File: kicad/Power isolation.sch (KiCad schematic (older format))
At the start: 0 parts

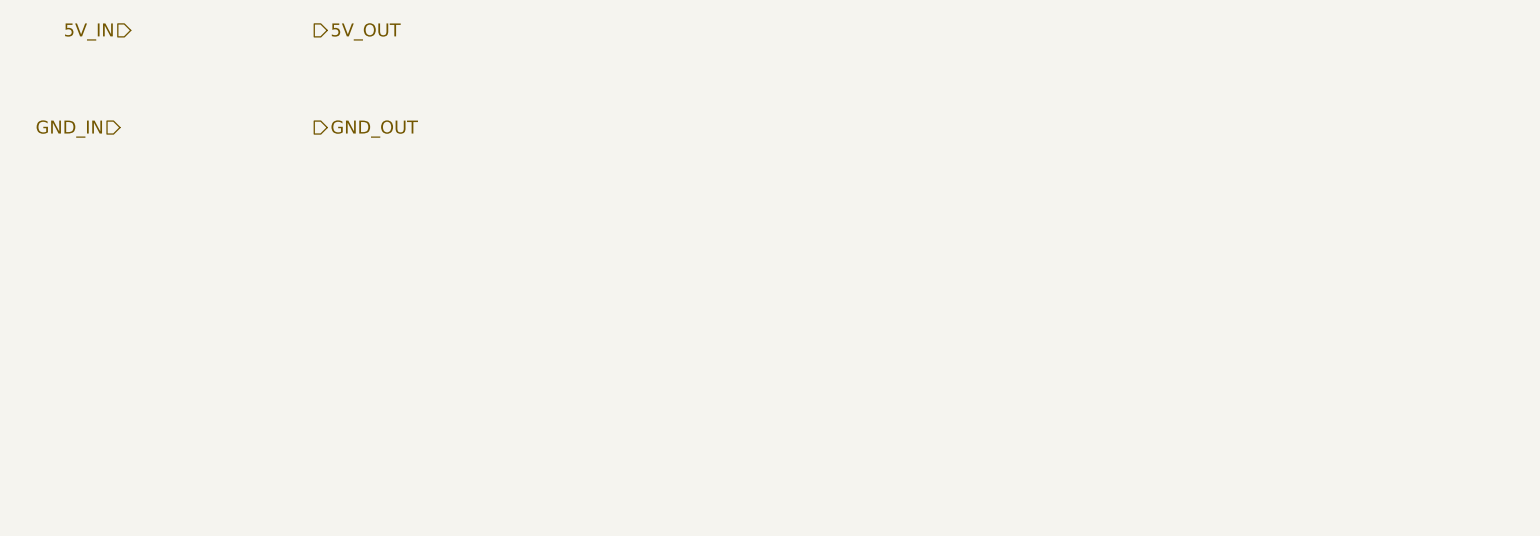
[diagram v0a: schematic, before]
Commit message: Completed data and power isolation sheets
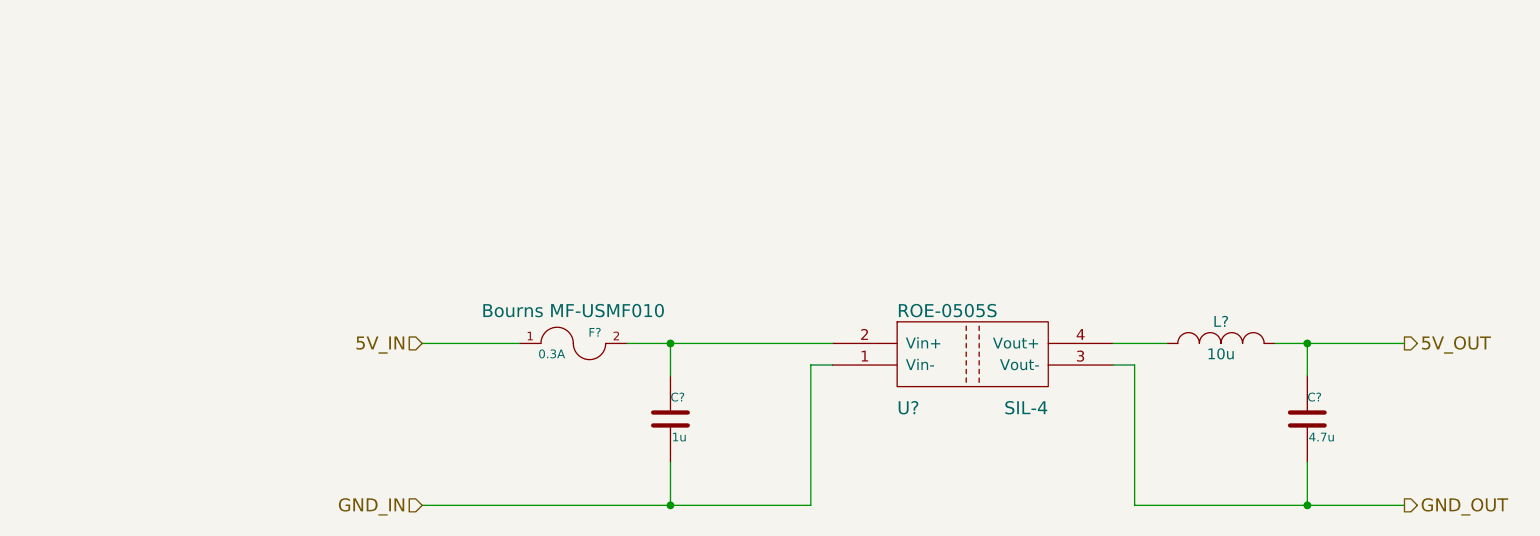
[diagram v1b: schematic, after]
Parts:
- added C?: 4.7u, ~, symbol C
- added C?: 1u, ~, symbol C
- added F?: 0.3A, ~, symbol FUSE
- added L?: 10u, ~, symbol INDUCTOR_SMALL
- added U?: ROE-0505S, SIL-4, symbol ROE-0505S
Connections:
- net 5V_IN: now also F?.1
- net 5V_OUT: now also C?.1, L?.2
- net GND_IN: now also C?.2, U?.1 (Vin-)
- net GND_OUT: now also C?.2, U?.3 (Vout-)
- new net: C?.1, F?.2, U?.2 (Vin+)
- new net: L?.1, U?.4 (Vout+)
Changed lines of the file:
@@
 LIBS:+5v_iso
 LIBS:gnd_iso
+LIBS:roe-0505s
+LIBS:si8660
 LIBS:Main-cache
 EELAYER 27 0
@@
 $Descr A4 11693 8268
 encoding utf-8
-Sheet 6 8
+Sheet 5 8
 Title ""
 Date "22 jun 2014"
@@
 Comment4 ""
 $EndDescr
-Text HLabel 2000 2150 0    60   Input ~ 0
+Text HLabel 3350 3600 0    60   Input ~ 0
 5V_IN
-Text HLabel 1950 2600 0    60   Input ~ 0
+Text HLabel 3350 4350 0    60   Input ~ 0
 GND_IN
-Text HLabel 2850 2150 2    60   Output ~ 0
+Text HLabel 7900 3600 2    60   Output ~ 0
 5V_OUT
-Text HLabel 2850 2600 2    60   Output ~ 0
+Text HLabel 7900 4350 2    60   Output ~ 0
 GND_OUT
+$Comp
+L ROE-0505S U?
+U 1 1 53AD64E4
+P 5900 3650
+F 0 "U?" H 5550 3400 60  0000 L CNN
+F 1 "ROE-0505S" H 5550 3850 60  0000 L CNN
+F 2 "SIL-4" H 6250 3400 60  0000 R CNN
+F 3 "" H 5900 3550 60  0000 C CNN
+	1    5900 3650
+	1    0    0    -1
+$EndComp
+$Comp
+L INDUCTOR_SMALL L?
+U 1 1 53AD651D
+P 7050 3600
+F 0 "L?" H 7050 3700 50  0000 C CNN
+F 1 "10u" H 7050 3550 50  0000 C CNN
+F 2 "~" H 7050 3600 60  0000 C CNN
+F 3 "~" H 7050 3600 60  0000 C CNN
+	1    7050 3600
+	1    0    0    -1
+$EndComp
+$Comp
+L C C?
+U 1 1 53AD6542
+P 7450 3950
+F 0 "C?" H 7450 4050 40  0000 L CNN
+F 1 "4.7u" H 7456 3865 40  0000 L CNN
+F 2 "~" H 7488 3800 30  0000 C CNN
+F 3 "~" H 7450 3950 60  0000 C CNN
+	1    7450 3950
+	1    0    0    -1
+$EndComp
+$Comp
+L C C?
+U 1 1 53AD6597
+P 4500 3950
+F 0 "C?" H 4500 4050 40  0000 L CNN
+F 1 "1u" H 4506 3865 40  0000 L CNN
+F 2 "~" H 4538 3800 30  0000 C CNN
+F 3 "~" H 4500 3950 60  0000 C CNN
+	1    4500 3950
+	1    0    0    -1
+$EndComp
+Wire Wire Line
+	4300 3600 4500 3600
+Wire Wire Line
+	4500 3600 5250 3600
+Wire Wire Line
+	5250 3700 5150 3700
+Wire Wire Line
+	7300 3600 7450 3600
+Wire Wire Line
+	7450 3600 7900 3600
+Wire Wire Line
+	6650 4350 7450 4350
+Wire Wire Line
+	7450 4350 7900 4350
+Wire Wire Line
+	7450 3750 7450 3600
+Connection ~ 7450 3600
+Wire Wire Line
+	6550 3600 6800 3600
+Wire Wire Line
+	6550 3700 6650 3700
+Wire Wire Line
+	6650 3700 6650 4350
+Wire Wire Line
+	7450 4150 7450 4350
+Connection ~ 7450 4350
+Wire Wire Line
+	5150 3700 5150 4350
+Wire Wire Line
+	5150 4350 4500 4350
+Wire Wire Line
+	4500 3600 4500 3750
+Wire Wire Line
+	4500 4150 4500 4350
+Connection ~ 4500 4350
+Connection ~ 4500 3600
+Wire Wire Line
+	3350 3600 3800 3600
+Wire Wire Line
+	4500 4350 3350 4350
+$Comp
+L FUSE F?
+U 1 1 53AD9F1B
+P 4050 3600
+F 0 "F?" H 4150 3650 40  0000 C CNN
+F 1 "0.3A" H 3950 3550 40  0000 C CNN
+F 2 "~" H 4050 3600 60  0000 C CNN
+F 3 "Bourns MF-USMF010" H 4050 3750 60  0000 C CNN
+	1    4050 3600
+	1    0    0    -1
+$EndComp
 $EndSCHEMATC

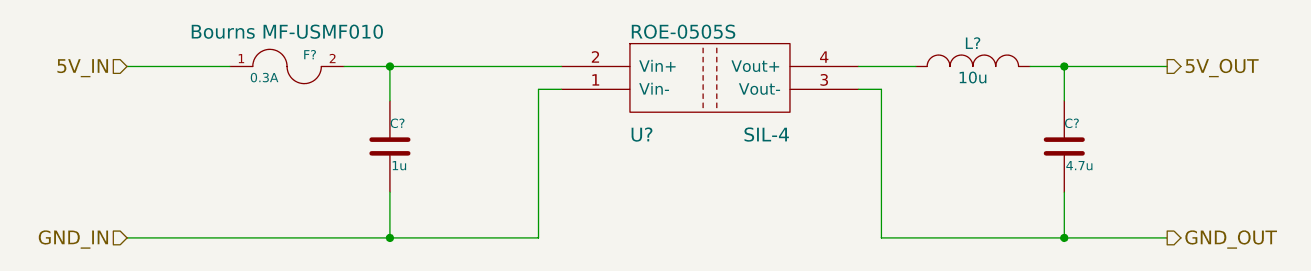
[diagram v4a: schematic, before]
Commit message: Netlist DRC pass - fixed pins types, incorrect connections, added PWRFLAGS
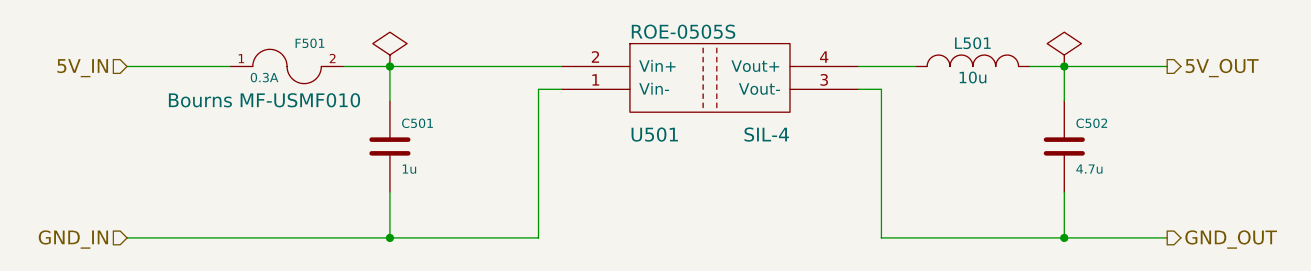
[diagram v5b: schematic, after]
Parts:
- gave numbers to parts that had none: 5
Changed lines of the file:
@@
 GND_OUT
 $Comp
-L ROE-0505S U?
+L ROE-0505S U501
 U 1 1 53AD64E4
 P 5900 3650
-F 0 "U?" H 5550 3400 60  0000 L CNN
+F 0 "U501" H 5550 3400 60  0000 L CNN
 F 1 "ROE-0505S" H 5550 3850 60  0000 L CNN
 F 2 "SIL-4" H 6250 3400 60  0000 R CNN
@@
 $EndComp
 $Comp
-L INDUCTOR_SMALL L?
+L INDUCTOR_SMALL L501
 U 1 1 53AD651D
 P 7050 3600
-F 0 "L?" H 7050 3700 50  0000 C CNN
+F 0 "L501" H 7050 3700 50  0000 C CNN
 F 1 "10u" H 7050 3550 50  0000 C CNN
 F 2 "~" H 7050 3600 60  0000 C CNN
@@
 $EndComp
 $Comp
-L C C?
+L C C502
 U 1 1 53AD6542
 P 7450 3950
-F 0 "C?" H 7450 4050 40  0000 L CNN
-F 1 "4.7u" H 7456 3865 40  0000 L CNN
+F 0 "C502" H 7500 4050 40  0000 L CNN
+F 1 "4.7u" H 7500 3850 40  0000 L CNN
 F 2 "~" H 7488 3800 30  0000 C CNN
 F 3 "~" H 7450 3950 60  0000 C CNN
@@
 $EndComp
 $Comp
-L C C?
+L C C501
 U 1 1 53AD6597
 P 4500 3950
-F 0 "C?" H 4500 4050 40  0000 L CNN
-F 1 "1u" H 4506 3865 40  0000 L CNN
+F 0 "C501" H 4550 4050 40  0000 L CNN
+F 1 "1u" H 4550 3850 40  0000 L CNN
 F 2 "~" H 4538 3800 30  0000 C CNN
 F 3 "~" H 4500 3950 60  0000 C CNN
@@
 $EndComp
 Wire Wire Line
-	4300 3600 4500 3600
-Wire Wire Line
-	4500 3600 5250 3600
+	4300 3600 5250 3600
 Wire Wire Line
 	5250 3700 5150 3700
 Wire Wire Line
-	7300 3600 7450 3600
+	7300 3600 7900 3600
 Wire Wire Line
-	7450 3600 7900 3600
-Wire Wire Line
-	6650 4350 7450 4350
-Wire Wire Line
-	7450 4350 7900 4350
+	6650 4350 7900 4350
 Wire Wire Line
 	7450 3750 7450 3600
@@
 	5150 3700 5150 4350
 Wire Wire Line
-	5150 4350 4500 4350
+	5150 4350 3350 4350
 Wire Wire Line
 	4500 3600 4500 3750
 Wire Wire Line
-	4500 4150 4500 4350
+	4500 4350 4500 4150
 Connection ~ 4500 4350
 Connection ~ 4500 3600
 Wire Wire Line
 	3350 3600 3800 3600
-Wire Wire Line
-	4500 4350 3350 4350
 $Comp
-L FUSE F?
+L FUSE F501
 U 1 1 53AD9F1B
 P 4050 3600
-F 0 "F?" H 4150 3650 40  0000 C CNN
+F 0 "F501" H 4150 3700 40  0000 C CNN
 F 1 "0.3A" H 3950 3550 40  0000 C CNN
 F 2 "~" H 4050 3600 60  0000 C CNN
-F 3 "Bourns MF-USMF010" H 4050 3750 60  0000 C CNN
+F 3 "Bourns MF-USMF010" H 3950 3450 60  0000 C CNN
 	1    4050 3600
 	1    0    0    -1
 $EndComp
+$Comp
+L PWR_FLAG #FLG502
+U 1 1 53C30EDC
+P 7450 3600
+F 0 "#FLG502" H 7450 3695 30  0001 C CNN
+F 1 "PWR_FLAG" H 7450 3780 30  0001 C CNN
+F 2 "" H 7450 3600 60  0000 C CNN
+F 3 "" H 7450 3600 60  0000 C CNN
+	1    7450 3600
+	1    0    0    -1
+$EndComp
+$Comp
+L PWR_FLAG #FLG501
+U 1 1 53C31C12
+P 4500 3600
+F 0 "#FLG501" H 4500 3695 30  0001 C CNN
+F 1 "PWR_FLAG" H 4500 3780 30  0001 C CNN
+F 2 "" H 4500 3600 60  0000 C CNN
+F 3 "" H 4500 3600 60  0000 C CNN
+	1    4500 3600
+	1    0    0    -1
+$EndComp
